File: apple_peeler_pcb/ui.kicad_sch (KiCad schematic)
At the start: 6 parts, among them SW3 SPST BTN

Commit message: replace fancy debug connectors by pin header to save $8
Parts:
- renumbered R42 to R43, R43 to R44
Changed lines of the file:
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@@
 		(dnp no)
 		(fields_autoplaced yes)
-		(property "Reference" "#PWR0108"
+		(property "Reference" "#PWR0106"
 			(at 184.15 125.73 0)
 			(effects
@@
 			(project "apple_peeler_pcb"
 				(path "/d5946b96-44a8-4a28-8641-19803e1510af/ff7927ce-242d-46a3-8944-ca0e798b7163"
-					(reference "#PWR0108")
+					(reference "#PWR0106")
 					(unit 1)
 				)
@@
 		(on_board yes)
 		(dnp no)
-		(property "Reference" "R42"
+		(property "Reference" "R43"
 			(at 142.24 129.54 90)
 			(effects
@@
 			(project "apple_peeler_pcb"
 				(path "/d5946b96-44a8-4a28-8641-19803e1510af/ff7927ce-242d-46a3-8944-ca0e798b7163"
-					(reference "R42")
+					(reference "R43")
 					(unit 1)
 				)
@@
 		(on_board yes)
 		(dnp no)
-		(property "Reference" "#PWR0103"
+		(property "Reference" "#PWR0101"
 			(at 135.89 132.08 0)
 			(effects
@@
 			(project "apple_peeler_pcb"
 				(path "/d5946b96-44a8-4a28-8641-19803e1510af/ff7927ce-242d-46a3-8944-ca0e798b7163"
-					(reference "#PWR0103")
+					(reference "#PWR0101")
 					(unit 1)
 				)
@@
 		(on_board yes)
 		(dnp no)
-		(property "Reference" "#PWR0109"
+		(property "Reference" "#PWR0107"
 			(at 213.36 105.41 0)
 			(effects
@@
 			(project "apple_peeler_pcb"
 				(path "/d5946b96-44a8-4a28-8641-19803e1510af/ff7927ce-242d-46a3-8944-ca0e798b7163"
-					(reference "#PWR0109")
+					(reference "#PWR0107")
 					(unit 1)
 				)
@@
 		(on_board yes)
 		(dnp no)
-		(property "Reference" "#PWR0107"
+		(property "Reference" "#PWR0105"
 			(at 184.15 105.41 0)
 			(effects
@@
 			(project "apple_peeler_pcb"
 				(path "/d5946b96-44a8-4a28-8641-19803e1510af/ff7927ce-242d-46a3-8944-ca0e798b7163"
-					(reference "#PWR0107")
+					(reference "#PWR0105")
 					(unit 1)
 				)
@@
 		(dnp no)
 		(fields_autoplaced yes)
-		(property "Reference" "#PWR0105"
+		(property "Reference" "#PWR0103"
 			(at 170.18 91.44 0)
 			(effects
@@
 			(project "apple_peeler_pcb"
 				(path "/d5946b96-44a8-4a28-8641-19803e1510af/ff7927ce-242d-46a3-8944-ca0e798b7163"
-					(reference "#PWR0105")
+					(reference "#PWR0103")
 					(unit 1)
 				)
@@
 		(dnp no)
 		(fields_autoplaced yes)
-		(property "Reference" "#PWR0106"
+		(property "Reference" "#PWR0104"
 			(at 170.18 132.08 0)
 			(effects
@@
 			(project "apple_peeler_pcb"
 				(path "/d5946b96-44a8-4a28-8641-19803e1510af/ff7927ce-242d-46a3-8944-ca0e798b7163"
-					(reference "#PWR0106")
+					(reference "#PWR0104")
 					(unit 1)
 				)
@@
 		(on_board yes)
 		(dnp no)
-		(property "Reference" "R43"
+		(property "Reference" "R44"
 			(at 140.97 82.5499 0)
 			(effects
@@
 			(project "apple_peeler_pcb"
 				(path "/d5946b96-44a8-4a28-8641-19803e1510af/ff7927ce-242d-46a3-8944-ca0e798b7163"
-					(reference "R43")
+					(reference "R44")
 					(unit 1)
 				)
@@
 		(dnp no)
 		(fields_autoplaced yes)
-		(property "Reference" "#PWR0110"
+		(property "Reference" "#PWR0108"
 			(at 213.36 125.73 0)
 			(effects
@@
 			(project "apple_peeler_pcb"
 				(path "/d5946b96-44a8-4a28-8641-19803e1510af/ff7927ce-242d-46a3-8944-ca0e798b7163"
-					(reference "#PWR0110")
+					(reference "#PWR0108")
 					(unit 1)
 				)
@@
 		(on_board yes)
 		(dnp no)
-		(property "Reference" "#PWR0104"
+		(property "Reference" "#PWR0102"
 			(at 143.51 82.55 0)
 			(effects
@@
 			(project "apple_peeler_pcb"
 				(path "/d5946b96-44a8-4a28-8641-19803e1510af/ff7927ce-242d-46a3-8944-ca0e798b7163"
-					(reference "#PWR0104")
-					(unit 1)
-				)
+					(reference "#PWR0102")
+					(unit 1)
+				)

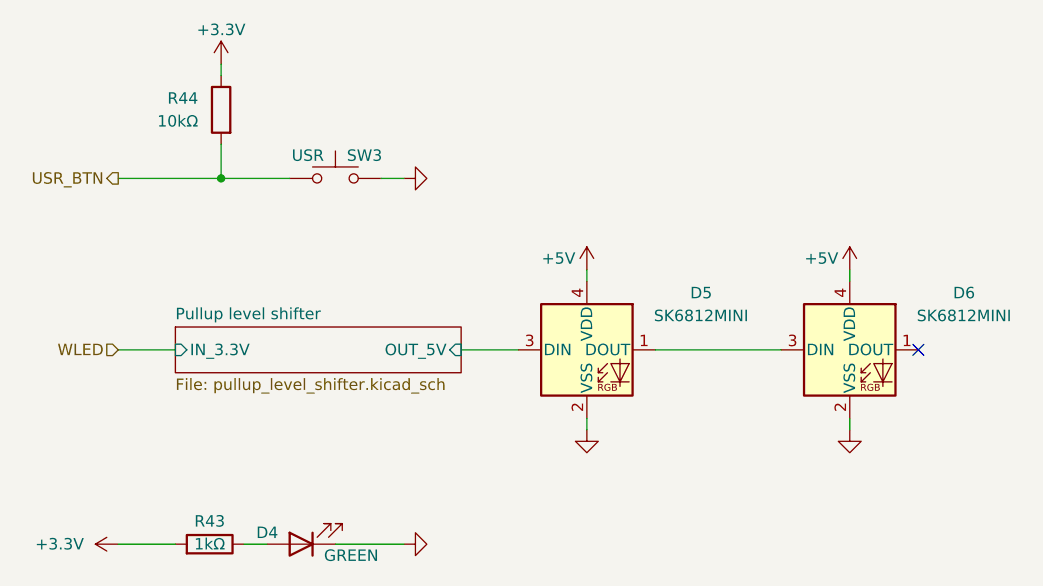
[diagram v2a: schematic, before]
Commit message: FUCKING HELL why is the kicad library symbol wrong
fix the pin order of rgb led symbol
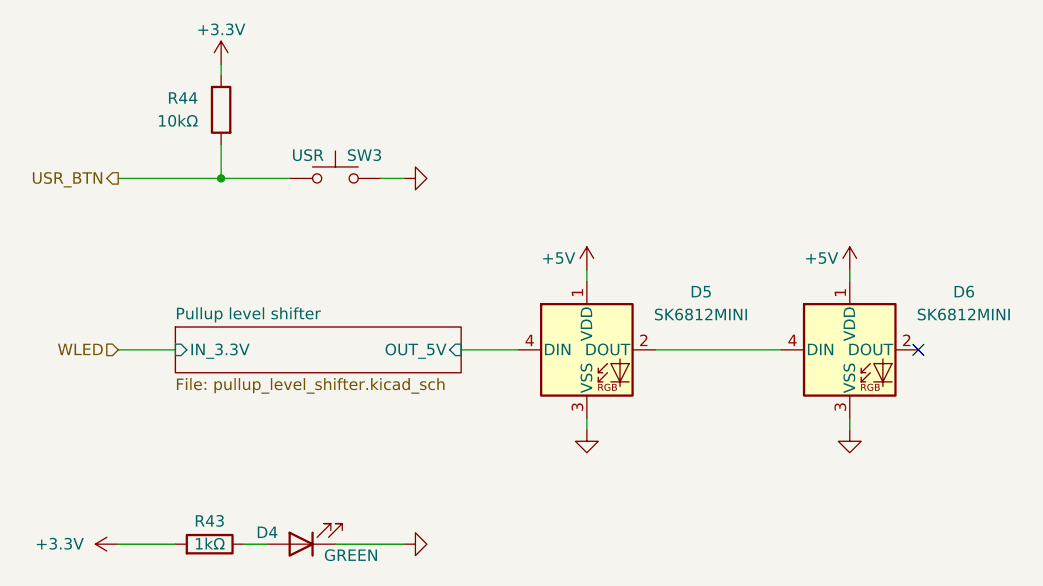
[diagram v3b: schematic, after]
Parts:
- D5, D6: symbol LED:SK6812MINI -> led:SK6812MINI
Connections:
- net +5V: now also D5.1 (VDD), D6.1 (VDD); no longer D5.4 (VDD), D6.4 (VDD)
- net GND: now also D5.3 (VSS), D6.3 (VSS); no longer D5.2 (VSS), D6.2 (VSS)
- net Pullup level shifter/OUT_5V: now also D5.4 (DIN); no longer D5.3 (DIN)
- new net: D5.2 (DOUT), D6.4 (DIN)
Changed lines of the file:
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@@
 	)
 	(symbol
-		(lib_id "LED:SK6812MINI")
+		(lib_id "led:SK6812MINI")
 		(at 213.36 110.49 0)
 		(unit 1)
@@
 		(fields_autoplaced yes)
 		(property "Reference" "D6"
-			(at 226.06 104.1714 0)
+			(at 226.06 104.0698 0)
 			(effects
 				(font
@@
 		)
 		(property "Value" "SK6812MINI"
-			(at 226.06 106.7114 0)
+			(at 226.06 106.6098 0)
 			(effects
 				(font
@@
 	)
 	(symbol
-		(lib_id "LED:SK6812MINI")
+		(lib_id "led:SK6812MINI")
 		(at 184.15 110.49 0)
 		(unit 1)
@@
 		(fields_autoplaced yes)
 		(property "Reference" "D5"
-			(at 196.85 104.1714 0)
+			(at 196.85 104.0698 0)
 			(effects
 				(font
@@
 		)
 		(property "Value" "SK6812MINI"
-			(at 196.85 106.7114 0)
-			(effects
-				(font
+			(at 196.85 106.6098 0)
+			(effects
+				(font

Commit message: fix the fucking WLED footprints
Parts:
- removed D5, D6: SK6812MINI, LED_SMD:LED_SK6812MINI_PLCC4_3.5x3.5mm_P1.75mm, symbol led:SK6812MINI
- added D5, D6: SK6812MINI-HS, leds:LED_SK6812MINI_HS_012, symbol LED:SK6812
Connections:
- net +5V: now also D5.3 (VDD), D6.3 (VDD)
- net GND: now also D5.1 (VSS), D6.1 (VSS)
- net Pullup level shifter/OUT_5V: now also D5.2 (DIN)
- new net: D5.4 (DOUT), D6.2 (DIN)
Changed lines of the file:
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@@
+	)
+	(symbol
+		(lib_id "LED:SK6812")
+		(at 184.15 110.49 0)
+		(unit 1)
+		(exclude_from_sim no)
+		(in_bom yes)
+		(on_board yes)
+		(dnp no)
+		(property "Reference" "D5"
+			(at 186.69 104.14 0)
+			(effects
+				(font
+					(size 1.27 1.27)
+				)
+			)
+		)
+		(property "Value" "SK6812MINI-HS"
+			(at 193.04 116.84 0)
+			(effects
+				(font
+					(size 1.27 1.27)
+				)
+			)
+		)
+		(property "Footprint" "leds:LED_SK6812MINI_HS_012"
+			(at 185.42 118.11 0)
+			(effects
+				(font
+					(size 1.27 1.27)
+				)
+				(justify left top)
+				(hide yes)
+			)
+		)
+		(property "Datasheet" "https://cdn-shop.adafruit.com/product-files/1138/SK6812+LED+datasheet+.pdf"
+			(at 186.69 120.015 0)
+			(effects
+				(font
+					(size 1.27 1.27)
+				)
+				(justify left top)
+				(hide yes)
+			)
+		)
+		(property "Description" "RGB LED with integrated controller"
+			(at 184.15 110.49 0)
+			(effects
+				(font
+					(size 1.27 1.27)
+				)
+				(hide yes)
+			)
+		)
+		(property "MPN" "SK6812MINI-HS"
+			(at 184.15 110.49 0)
+			(effects
+				(font
+					(size 1.27 1.27)
+				)
+				(hide yes)
+			)
+		)
+		(property "LCSC" "C2922787"
+			(at 184.15 110.49 0)
+			(effects
+				(font
+					(size 1.27 1.27)
+				)
+				(hide yes)
+			)
+		)
+		(pin "4"
+		)
+		(pin "1"
+		)
+		(pin "3"
+		)
+		(pin "2"
+		)
+		(instances
+			(project ""
+				(path "/d5946b96-44a8-4a28-8641-19803e1510af/ff7927ce-242d-46a3-8944-ca0e798b7163"
+					(reference "D5")
+					(unit 1)
+				)
+			)
+		)
 	)
 	(symbol
@@
 				(path "/d5946b96-44a8-4a28-8641-19803e1510af/ff7927ce-242d-46a3-8944-ca0e798b7163"
 					(reference "#PWR0101")
-					(unit 1)
-				)
-			)
-		)
-	)
-	(symbol
-		(lib_id "led:SK6812MINI")
-		(at 213.36 110.49 0)
-		(unit 1)
-		(exclude_from_sim no)
-		(in_bom yes)
-		(on_board yes)
-		(dnp no)
-		(fields_autoplaced yes)
-		(property "Reference" "D6"
-			(at 226.06 104.0698 0)
-			(effects
-				(font
-					(size 1.27 1.27)
-				)
-			)
-		)
-		(property "Value" "SK6812MINI"
-			(at 226.06 106.6098 0)
-			(effects
-				(font
-					(size 1.27 1.27)
-				)
-			)
-		)
-		(property "Footprint" "LED_SMD:LED_SK6812MINI_PLCC4_3.5x3.5mm_P1.75mm"
-			(at 214.63 118.11 0)
-			(effects
-				(font
-					(size 1.27 1.27)
-				)
-				(justify left top)
-				(hide yes)
-			)
-		)
-		(property "Datasheet" "https://cdn-shop.adafruit.com/product-files/2686/SK6812MINI_REV.01-1-2.pdf"
-			(at 215.9 120.015 0)
-			(effects
-				(font
-					(size 1.27 1.27)
-				)
-				(justify left top)
-				(hide yes)
-			)
-		)
-		(property "Description" "RGB LED with integrated controller"
-			(at 213.36 110.49 0)
-			(effects
-				(font
-					(size 1.27 1.27)
-				)
-				(hide yes)
-			)
-		)
-		(property "Part" ""
-			(at 213.36 110.49 0)
-			(effects
-				(font
-					(size 1.27 1.27)
-				)
-				(hide yes)
-			)
-		)
-		(property "LCSC" "C5149201"
-			(at 213.36 110.49 0)
-			(effects
-				(font
-					(size 1.27 1.27)
-				)
-				(hide yes)
-			)
-		)
-		(property "MPN" "SK6812MINI-E"
-			(at 213.36 110.49 0)
-			(effects
-				(font
-					(size 1.27 1.27)
-				)
-				(hide yes)
-			)
-		)
-		(pin "2"
-		)
-		(pin "4"
-		)
-		(pin "3"
-		)
-		(pin "1"
-		)
-		(instances
-			(project "apple_peeler_pcb"
-				(path "/d5946b96-44a8-4a28-8641-19803e1510af/ff7927ce-242d-46a3-8944-ca0e798b7163"
-					(reference "D6")
 					(unit 1)
 				)
@@
 	)
 	(symbol
-		(lib_id "led:SK6812MINI")
-		(at 184.15 110.49 0)
-		(unit 1)
-		(exclude_from_sim no)
-		(in_bom yes)
-		(on_board yes)
-		(dnp no)
-		(fields_autoplaced yes)
-		(property "Reference" "D5"
-			(at 196.85 104.0698 0)
-			(effects
-				(font
-					(size 1.27 1.27)
-				)
-			)
-		)
-		(property "Value" "SK6812MINI"
-			(at 196.85 106.6098 0)
-			(effects
-				(font
-					(size 1.27 1.27)
-				)
-			)
-		)
-		(property "Footprint" "LED_SMD:LED_SK6812MINI_PLCC4_3.5x3.5mm_P1.75mm"
-			(at 185.42 118.11 0)
-			(effects
-				(font
-					(size 1.27 1.27)
-				)
-				(justify left top)
-				(hide yes)
-			)
-		)
-		(property "Datasheet" "https://cdn-shop.adafruit.com/product-files/2686/SK6812MINI_REV.01-1-2.pdf"
-			(at 186.69 120.015 0)
-			(effects
-				(font
-					(size 1.27 1.27)
-				)
-				(justify left top)
-				(hide yes)
-			)
-		)
-		(property "Description" "RGB LED with integrated controller"
-			(at 184.15 110.49 0)
-			(effects
-				(font
-					(size 1.27 1.27)
-				)
-				(hide yes)
-			)
-		)
-		(property "Part" ""
-			(at 184.15 110.49 0)
-			(effects
-				(font
-					(size 1.27 1.27)
-				)
-				(hide yes)
-			)
-		)
-		(property "LCSC" "C5149201"
-			(at 184.15 110.49 0)
-			(effects
-				(font
-					(size 1.27 1.27)
-				)
-				(hide yes)
-			)
-		)
-		(property "MPN" "SK6812MINI-E"
-			(at 184.15 110.49 0)
-			(effects
-				(font
-					(size 1.27 1.27)
-				)
-				(hide yes)
-			)
-		)
-		(pin "2"
-		)
-		(pin "4"
-		)
-		(pin "3"
-		)
-		(pin "1"
-		)
-		(instances
-			(project "apple_peeler_pcb"
-				(path "/d5946b96-44a8-4a28-8641-19803e1510af/ff7927ce-242d-46a3-8944-ca0e798b7163"
-					(reference "D5")
-					(unit 1)
-				)
-			)
-		)
-	)
-	(symbol
 		(lib_id "power:GND")
 		(at 213.36 119.38 0)
@@
 					(unit 1)
 				)
+			)
+		)
+	)
+	(symbol
+		(lib_id "LED:SK6812")
+		(at 213.36 110.49 0)
+		(unit 1)
+		(exclude_from_sim no)
+		(in_bom yes)
+		(on_board yes)
+		(dnp no)
+		(property "Reference" "D6"
+			(at 215.9 104.14 0)
+			(effects
+				(font
+					(size 1.27 1.27)
+				)
+			)
+		)
+		(property "Value" "SK6812MINI-HS"
+			(at 222.25 116.84 0)
+			(effects
+				(font
+					(size 1.27 1.27)
+				)
+			)
+		)
+		(property "Footprint" "leds:LED_SK6812MINI_HS_012"
+			(at 214.63 118.11 0)
+			(effects
+				(font
+					(size 1.27 1.27)
+				)
+				(justify left top)
+				(hide yes)
+			)
+		)
+		(property "Datasheet" "https://cdn-shop.adafruit.com/product-files/1138/SK6812+LED+datasheet+.pdf"
+			(at 215.9 120.015 0)
+			(effects
+				(font
+					(size 1.27 1.27)
+				)
+				(justify left top)
+				(hide yes)
+			)
+		)
+		(property "Description" "RGB LED with integrated controller"
+			(at 213.36 110.49 0)
+			(effects
+				(font
+					(size 1.27 1.27)
+				)
+				(hide yes)
+			)
+		)
+		(property "MPN" "SK6812MINI-HS"
+			(at 213.36 110.49 0)
+			(effects
+				(font
+					(size 1.27 1.27)
+				)
+				(hide yes)
+			)
+		)
+		(property "LCSC" "C2922787"
+			(at 213.36 110.49 0)
+			(effects
+				(font
+					(size 1.27 1.27)
+				)
+				(hide yes)
+			)
+		)
+		(pin "4"
+		)
+		(pin "1"
+		)
+		(pin "3"
+		)
+		(pin "2"
+		)
+		(instances
+			(project "apple_peeler_pcb"
+				(path "/d5946b96-44a8-4a28-8641-19803e1510af/ff7927ce-242d-46a3-8944-ca0e798b7163"
+					(reference "D6")
+					(unit 1)
+				)
